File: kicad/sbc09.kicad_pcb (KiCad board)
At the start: 4 copper layers, 160 x 100 mm, 75 parts, among them J1 Conn_01x04_Male, J2 Conn_01x06_Male, J3 Conn_01x06_Male, J4 Conn_01x06_Male, J5 Conn_02x05_Odd_Even, J6 Conn_02x25_Odd_Even, J7 Conn_02x05_Odd_Even, Q1 2N7000, SW1 SW_Push, U1 74HCT245, U10 SST39SF040-DIP, U11 XR68C681CJ, U12 MAX232, U2 74HCT245, U3 74HCT245, U4 MC6809E, U5 74HCT125, U6 EPM7128SLC84, U7 71256SA15TPG, U8 AS6C4008-55PCN, U9 SST39SF040-DIP, X1 8MHz, X2 3.6864MHz

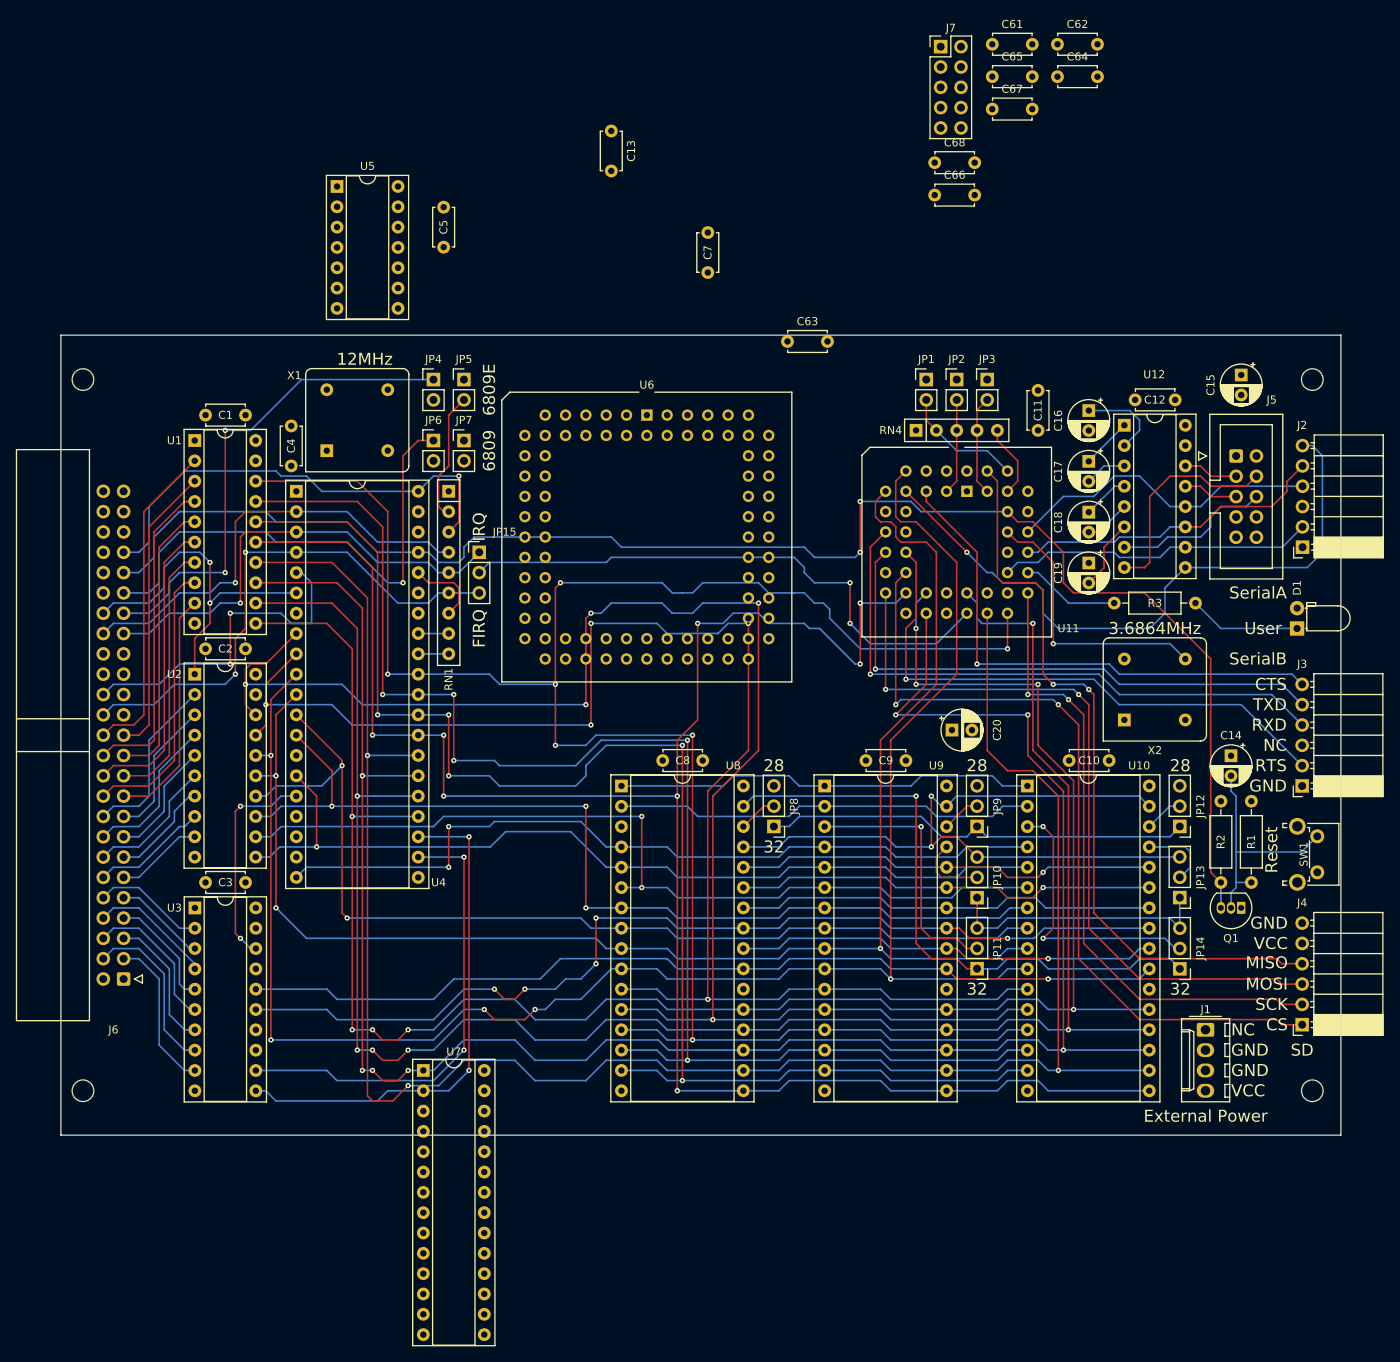
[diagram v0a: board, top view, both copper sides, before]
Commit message: CPLD pinout firmed up
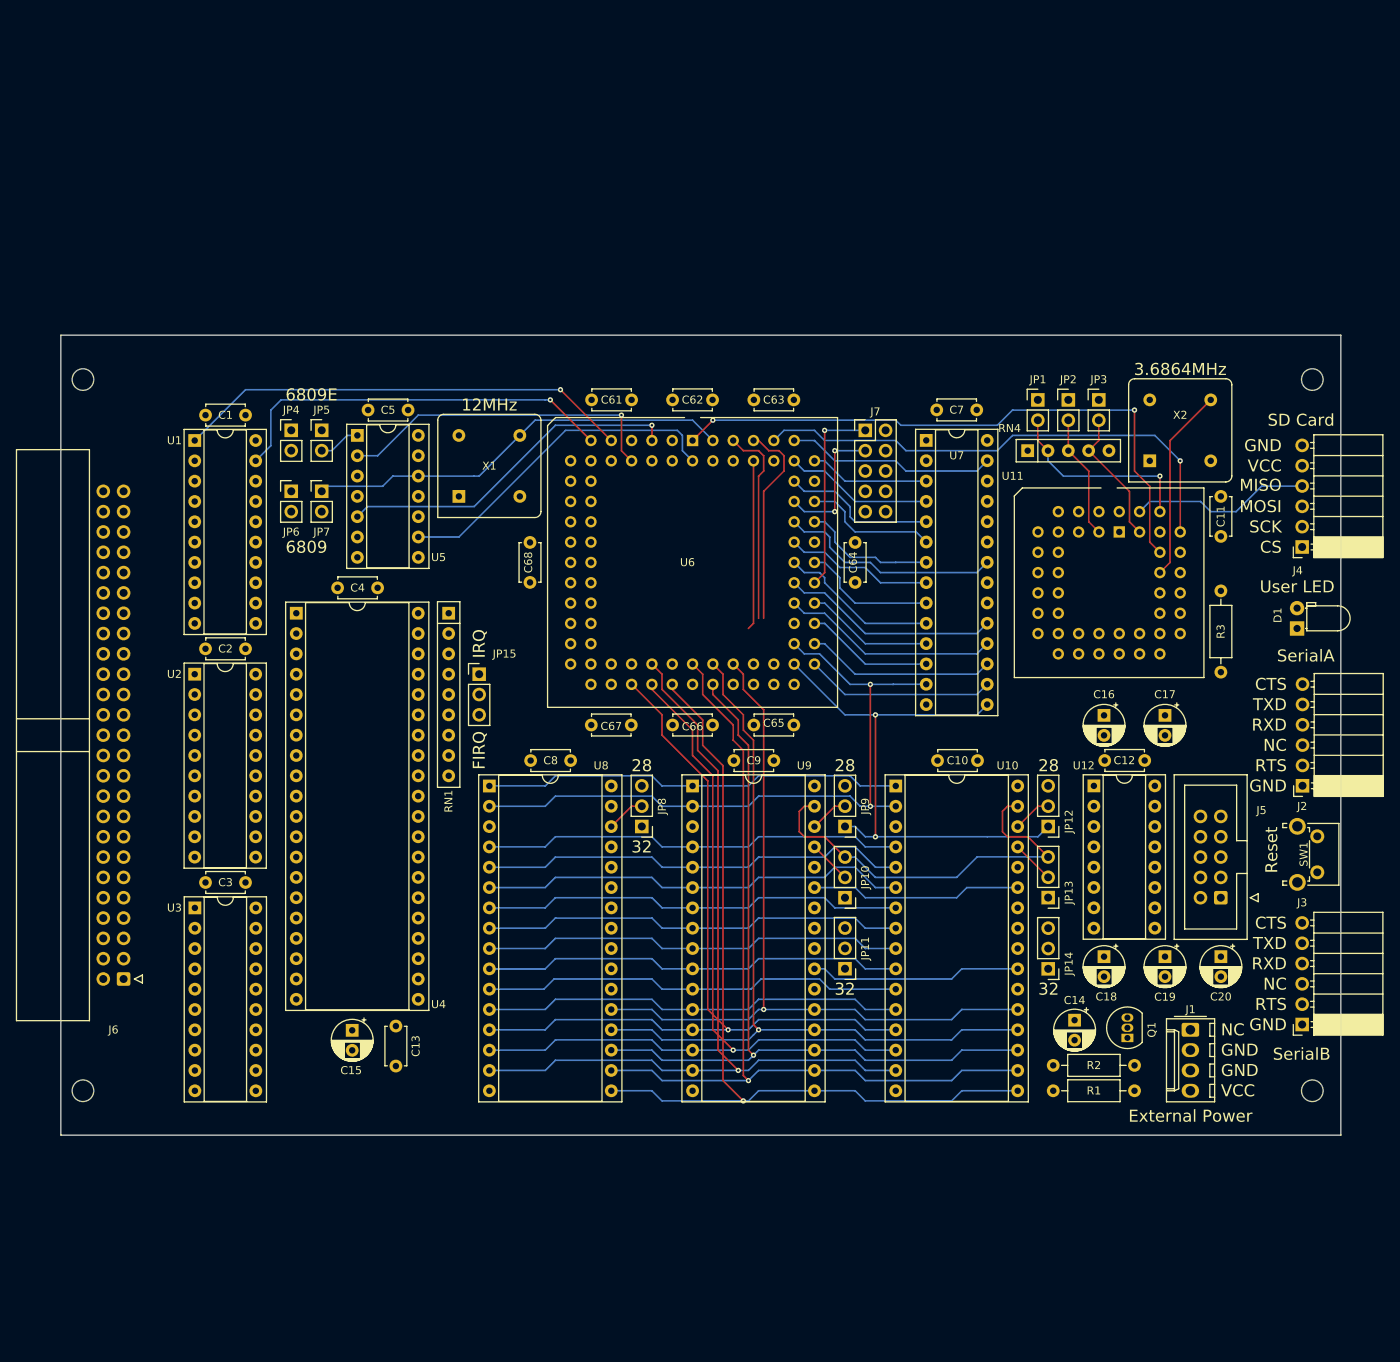
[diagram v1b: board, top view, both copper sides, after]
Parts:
- moved C15 138.1 mm to (114.9, 139.8)
- moved C13 115.1 mm to (120.4, 139.2)
- moved U7 100.8 mm to (186.7, 66.0)
- moved C67 91.9 mm to (144.8, 101.6)
- moved C65 86.3 mm to (165.1, 101.6)
- moved C66 73.9 mm to (155.0, 101.6)
- moved C68 72.9 mm to (137.2, 83.8), turned to 90 degrees
- moved C64 68.1 mm to (177.8, 83.8), turned to 90 degrees
- moved C61 67.0 mm to (144.9, 61.0)
- moved C62 65.5 mm to (155.0, 61.0)
- moved J4 59.7 mm to (233.7, 79.3)
- moved C18 55.6 mm to (208.9, 130.6)
- moved J5 55.2 mm to (223.5, 123.2), turned to 180 degrees
- moved C19 50.1 mm to (216.5, 130.6)
- moved J7 48.9 mm to (179.1, 64.8)
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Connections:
- U5 pad 5: Net-(U6-Pad4) -> Net-(U5-Pad5)
- U6 pad 1: (no net) -> nRST
- U6 pad 10: (no net) -> MRDY
- U6 pad 11: (no net) -> nBUFEN
- U6 pad 12: (no net) -> BS
- U6 pad 15: (no net) -> BA
- U6 pad 16: (no net) -> RnW
- U6 pad 17: (no net) -> /A0
- U6 pad 18: (no net) -> /A1
- U6 pad 20: (no net) -> /A2
- U6 pad 21: (no net) -> /A3
- U6 pad 22: (no net) -> /A4
- U6 pad 24: (no net) -> /A5
- U6 pad 25: (no net) -> /A6
- U6 pad 27: (no net) -> /A7
- U6 pad 28: (no net) -> /A8
- U6 pad 29: (no net) -> /A9
- U6 pad 30: (no net) -> /A10
- U6 pad 31: (no net) -> /A11
- U6 pad 33: (no net) -> /A13
- U6 pad 34: (no net) -> /A12
- U6 pad 35: (no net) -> /A15
- U6 pad 36: (no net) -> /A14
- U6 pad 37: (no net) -> /D0
- U6 pad 39: (no net) -> /D1
- U6 pad 4: /A0 -> nCSEXT
- U6 pad 40: (no net) -> /D2
- U6 pad 41: (no net) -> /D3
- U6 pad 44: (no net) -> /D4
- U6 pad 45: (no net) -> /D5
- U6 pad 46: (no net) -> /D6
- U6 pad 48: (no net) -> /D7
- U6 pad 49: (no net) -> nRD
- U6 pad 5: BA -> Net-(U5-Pad5)
- U6 pad 50: (no net) -> /A8X
- U6 pad 51: (no net) -> nWR
- U6 pad 52: (no net) -> /QA13
- U6 pad 54: (no net) -> /QA18
- U6 pad 55: (no net) -> /QA17
- U6 pad 56: (no net) -> /QA19
- U6 pad 57: (no net) -> /QA16
- U6 pad 58: (no net) -> /QA15
- U6 pad 6: (no net) -> unconnected-(U6-Pad6)
- U6 pad 60: (no net) -> /QA14
- U6 pad 61: (no net) -> /QA20
- U6 pad 63: (no net) -> /QA21
- U6 pad 64: (no net) -> /MMU_A1
- U6 pad 65: (no net) -> /MMU_A0
- U6 pad 67: (no net) -> /MMU_A2
- U6 pad 68: (no net) -> /MMU_A3
- U6 pad 69: (no net) -> /MMU_nRD
- U6 pad 70: (no net) -> /MMU_A4
- U6 pad 73: (no net) -> /MMU_A5
- U6 pad 74: (no net) -> /MMU_A7
- U6 pad 75: (no net) -> /MMU_nWR
- U6 pad 76: (no net) -> /MMU_A6
- U6 pad 77: (no net) -> nCSUART
- U6 pad 79: (no net) -> nCSROM1
- U6 pad 8: (no net) -> Net-(U5-Pad2)
- U6 pad 80: (no net) -> nCSRAM
- U6 pad 81: (no net) -> nCSROM0
- U6 pad 83: (no net) -> CLKX4
- U6 pad 84: CLKX4 -> unconnected-(U6-Pad84)
- U6 pad 9: (no net) -> BUFDIR
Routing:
- net /A2: track 222.1 -> 59.9 mm, vias 5 -> 0
- net /D5: track 259.7 -> 101.4 mm, vias 7 -> 1
- net /D0: track 254.6 -> 101.1 mm, vias 7 -> 1
- net /D7: track 245.9 -> 97.7 mm, vias 8 -> 1
- net /A0: track 199.5 -> 52.9 mm, vias 5 -> 0
- net /D4: track 251.9 -> 107.9 mm, vias 3 -> 1
- net /D6: track 244.3 -> 101.0 mm, vias 6 -> 1
- net /A3: track 194.7 -> 52.9 mm, vias 3 -> 0
- net /A1: track 189.3 -> 53.2 mm, vias 5 -> 0
- net /D3: track 240.5 -> 108.7 mm, vias 8 -> 1
- net /A11: track 124.5 -> 0.00 mm, vias 5 -> 0
- net nRST: track 194.9 -> 76.4 mm
- net /SDCS: track 102.0 -> 0.00 mm, vias 2 -> 0
- net /SDMOSI: track 95.8 -> 0.00 mm, vias 2 -> 0
- net /A10: track 116.9 -> 26.5 mm, vias 1 -> 0
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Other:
- board text added: "SD Card"
- board text added: "User LED"
- board text removed: "SD"
- board text removed: "User"
